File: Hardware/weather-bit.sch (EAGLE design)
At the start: 39 parts, among them J2 RJ11, J3 RJ11, U1 BME280, U2 micro:bit

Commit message: Updated One-Wire Hardware Set-up
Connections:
- removed net 13: U2.P13
- net 3.3V: now also R11.1; no longer R11.2
- net TEMP_DAT: now also R11.2, U2.P13; no longer R11.1
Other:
- moved on the sheet: J4, J5, J6, J7, R11

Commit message: Updating weather:bit per QC review
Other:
- note added: "v10"
- note removed: "v01"
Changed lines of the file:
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@@
 <sheet>
 <plain>
-<text x="238.76" y="7.62" size="2.54" layer="94">v01</text>
+<text x="238.76" y="7.62" size="2.54" layer="94">v10</text>
 <text x="5.08" y="175.26" size="5.08" layer="97">CONNECTOR</text>
 <text x="149.86" y="93.98" size="1.778" layer="97">20
@@
 <wire x1="58.42" y1="68.58" x2="58.42" y2="0" width="0.1524" layer="97" style="longdash"/>
 <text x="167.64" y="10.16" size="1.778" layer="94">Mary West, based on Weather Shield design by Nathan Seidle</text>
-<text x="241.3" y="7.62" size="1.778" layer="94">v01</text>
+<text x="241.3" y="7.62" size="1.778" layer="94">v10</text>
 </plain>
 <instances>

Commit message: Updated text in sch
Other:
- note added: "Intended to mate with OpenLog"
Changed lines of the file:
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@@
 <text x="167.64" y="10.16" size="1.778" layer="94">Mary West, based on Weather Shield design by Nathan Seidle</text>
 <text x="241.3" y="7.62" size="1.778" layer="94">v10</text>
+<text x="10.16" y="20.32" size="1.778" layer="97">Intended to mate with OpenLog</text>
 </plain>
 <instances>

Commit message: Added qwiic connector and logos
- added vertical qwiic connector near the 4-pin I2C header
- added qwiic logo near connector
- added big qwiic logos near product names on top and bottom silk
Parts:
- added J8: Qwiic (vertical), SparkFun-Connectors:QWIIC_CONNECTOR
- J9: value (none) -> PTH
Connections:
- net 3.3V: now also J8.2
- net GND: now also J8.1
- net SCL: now also J8.4
- net SDA: now also J8.3
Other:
- note added: "v11"
- moved on the sheet: J9

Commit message: SMD connector on 40 pin RA, and 4-pin I2C header
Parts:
- J6, J7: value (none) -> 455-1750-1-ND
- J9: value PTH -> 1X04_SMD_STRAIGHT_COMBO; device SparkFun-Connectors:CONN_041X04_NO_SILK -> SparkFun-Connectors:CONN_04SMD_STRAIGHT_COMBO
- U2: device Micro_Bit_Parts:MICRO:BITLEDS_UP -> SparkFun-Connectors:MICRO:BIT_RA
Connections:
- new net N$3: U2.P13
- net TEMP_DAT: no longer U2.P13

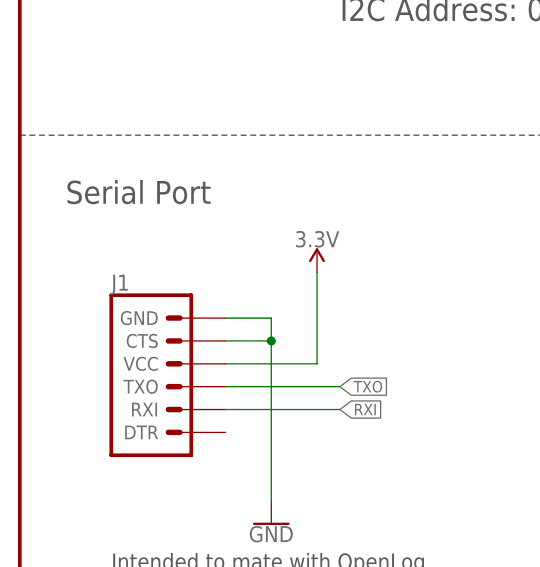
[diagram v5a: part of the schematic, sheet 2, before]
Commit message: Moved to SMT vertical female header for Serial port
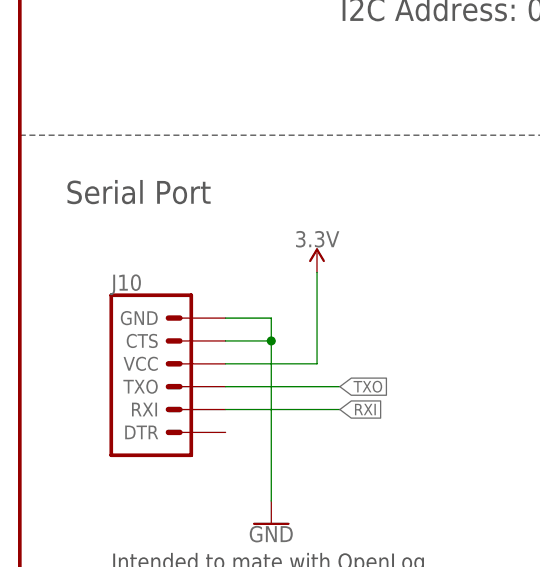
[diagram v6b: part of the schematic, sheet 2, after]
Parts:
- removed J1: (no value), SparkFun-Connectors:6_PIN_SERIAL_TARGETSILK
- added J10: (no value), SparkFun-Connectors:6_PIN_SERIAL_TARGETVERT_SMT
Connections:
- net 3.3V: now also J10.VCC; no longer J1.VCC
- net GND: now also J10.CTS, J10.GND; no longer J1.CTS, J1.GND
- net RXI: now also J10.RXI; no longer J1.RXI
- net TXO: now also J10.TXO; no longer J1.TXO
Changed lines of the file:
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@@
 <part name="SUPPLY8" library="SparkFun-PowerSymbols" deviceset="3.3V" device=""/>
 <part name="GND4" library="SparkFun-PowerSymbols" deviceset="GND" device=""/>
-<part name="J1" library="SparkFun-Connectors" deviceset="6_PIN_SERIAL_TARGET" device="SILK"/>
 <part name="SUPPLY1" library="SparkFun-PowerSymbols" deviceset="3.3V" device=""/>
 <part name="J8" library="SparkFun-Connectors" deviceset="QWIIC_CONNECTOR" device="" value="Qwiic (vertical)"/>
@@
 <part name="GND1" library="SparkFun-PowerSymbols" deviceset="GND" device=""/>
 <part name="U2" library="SparkFun-Connectors" deviceset="MICRO:BIT*?" device="_RA" value="micro:bit"/>
+<part name="J10" library="SparkFun-Connectors" deviceset="6_PIN_SERIAL_TARGET" device="VERT_SMT"/>
 </parts>
 <sheets>
@@
 <attribute name="VALUE" x="86.36" y="17.526" size="1.778" layer="96" align="top-center"/>
 </instance>
-<instance part="J1" gate="G$1" x="17.78" y="40.64" smashed="yes">
-<attribute name="VALUE" x="10.16" y="30.734" size="1.778" layer="96" font="vector"/>
-<attribute name="NAME" x="10.16" y="51.308" size="1.778" layer="95" font="vector"/>
-</instance>
 <instance part="SUPPLY1" gate="G$1" x="144.78" y="119.38" smashed="yes">
 <attribute name="VALUE" x="144.78" y="122.174" size="1.778" layer="96" align="bottom-center"/>
@@
 <instance part="GND1" gate="1" x="127" y="17.78" smashed="yes">
 <attribute name="VALUE" x="127" y="17.526" size="1.778" layer="96" align="top-center"/>
+</instance>
+<instance part="J10" gate="G$1" x="17.78" y="40.64" smashed="yes">
+<attribute name="VALUE" x="10.16" y="30.734" size="1.778" layer="96" font="vector"/>
+<attribute name="NAME" x="10.16" y="51.308" size="1.778" layer="95" font="vector"/>
 </instance>
 </instances>
@@
 </segment>
 <segment>
-<pinref part="J1" gate="G$1" pin="GND"/>
 <wire x1="22.86" y1="48.26" x2="27.94" y2="48.26" width="0.1524" layer="91"/>
 <wire x1="27.94" y1="48.26" x2="27.94" y2="45.72" width="0.1524" layer="91"/>
 <pinref part="GND2" gate="1" pin="GND"/>
-<pinref part="J1" gate="G$1" pin="CTS"/>
 <wire x1="27.94" y1="45.72" x2="27.94" y2="27.94" width="0.1524" layer="91"/>
 <wire x1="22.86" y1="45.72" x2="27.94" y2="45.72" width="0.1524" layer="91"/>
 <junction x="27.94" y="45.72"/>
+<pinref part="J10" gate="G$1" pin="CTS"/>
+<pinref part="J10" gate="G$1" pin="GND"/>
 </segment>
 <segment>
@@
 </segment>
 <segment>
-<pinref part="J1" gate="G$1" pin="VCC"/>
 <wire x1="22.86" y1="43.18" x2="33.02" y2="43.18" width="0.1524" layer="91"/>
 <pinref part="SUPPLY11" gate="G$1" pin="3.3V"/>
 <wire x1="33.02" y1="43.18" x2="33.02" y2="53.34" width="0.1524" layer="91"/>
+<pinref part="J10" gate="G$1" pin="VCC"/>
 </segment>
 <segment>
@@
 <net name="TXO" class="0">
 <segment>
-<pinref part="J1" gate="G$1" pin="TXO"/>
 <wire x1="22.86" y1="40.64" x2="35.56" y2="40.64" width="0.1524" layer="91"/>
 <label x="35.56" y="40.64" size="1.27" layer="95" font="vector" xref="yes"/>
+<pinref part="J10" gate="G$1" pin="TXO"/>
 </segment>
 </net>
 <net name="RXI" class="0">
 <segment>
-<pinref part="J1" gate="G$1" pin="RXI"/>
 <wire x1="22.86" y1="38.1" x2="35.56" y2="38.1" width="0.1524" layer="91"/>
 <label x="35.56" y="38.1" size="1.27" layer="95" font="vector" xref="yes"/>
-</segment>
-</net>
+<pinref part="J10" gate="G$1" pin="RXI"/>
+</segment>
+</net>

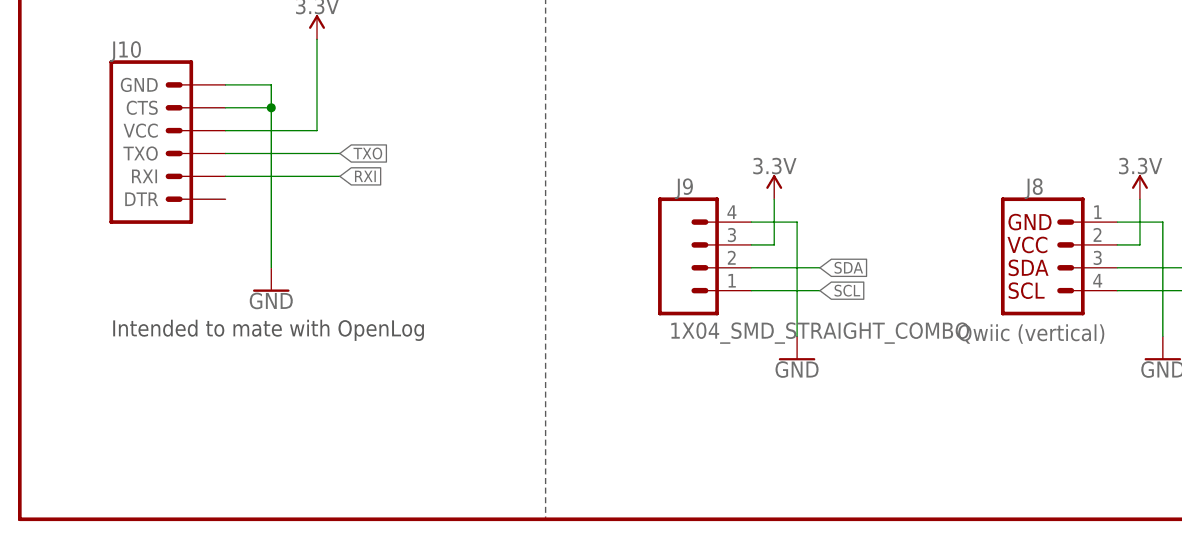
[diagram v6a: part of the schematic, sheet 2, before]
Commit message: SMT serial header and buzzard silk update
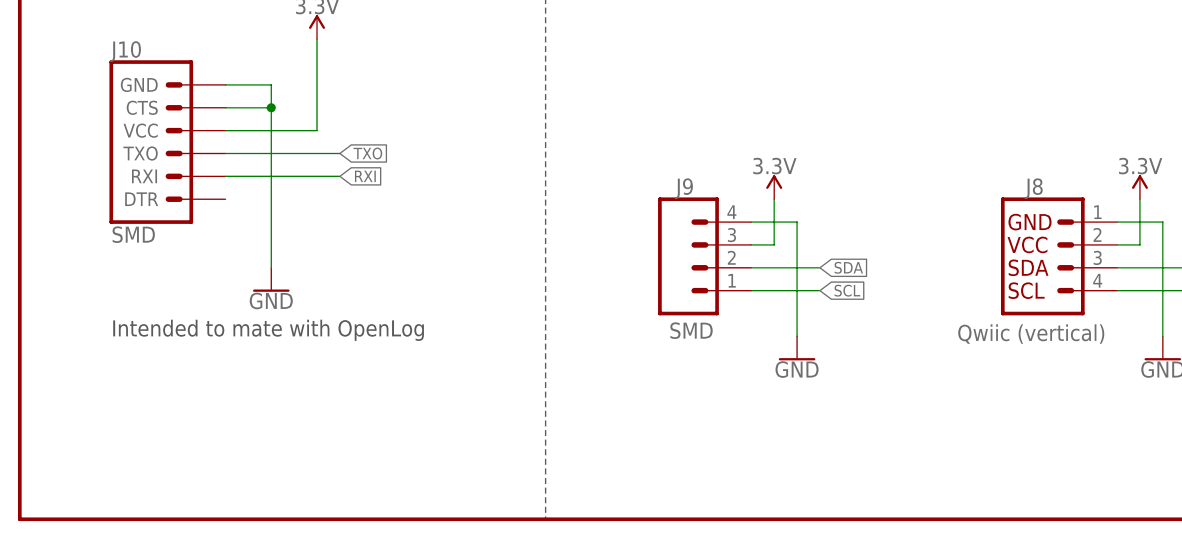
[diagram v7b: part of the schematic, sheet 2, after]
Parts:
- J10: value (none) -> SMD
- J9: value 1X04_SMD_STRAIGHT_COMBO -> SMD
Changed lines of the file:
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@@
 <part name="SUPPLY9" library="SparkFun-PowerSymbols" deviceset="3.3V" device=""/>
 <part name="SUPPLY10" library="SparkFun-PowerSymbols" deviceset="3.3V" device=""/>
-<part name="J9" library="SparkFun-Connectors" deviceset="CONN_04" device="SMD_STRAIGHT_COMBO" value="1X04_SMD_STRAIGHT_COMBO"/>
+<part name="J9" library="SparkFun-Connectors" deviceset="CONN_04" device="SMD_STRAIGHT_COMBO" value="SMD"/>
 <part name="SUPPLY11" library="SparkFun-PowerSymbols" deviceset="3.3V" device=""/>
 <part name="GND2" library="SparkFun-PowerSymbols" deviceset="GND" device=""/>
@@
 <part name="GND1" library="SparkFun-PowerSymbols" deviceset="GND" device=""/>
 <part name="U2" library="SparkFun-Connectors" deviceset="MICRO:BIT*?" device="_RA" value="micro:bit"/>
-<part name="J10" library="SparkFun-Connectors" deviceset="6_PIN_SERIAL_TARGET" device="VERT_SMT"/>
+<part name="J10" library="SparkFun-Connectors" deviceset="6_PIN_SERIAL_TARGET" device="VERT_SMT" value="SMD"/>
 </parts>
 <sheets>

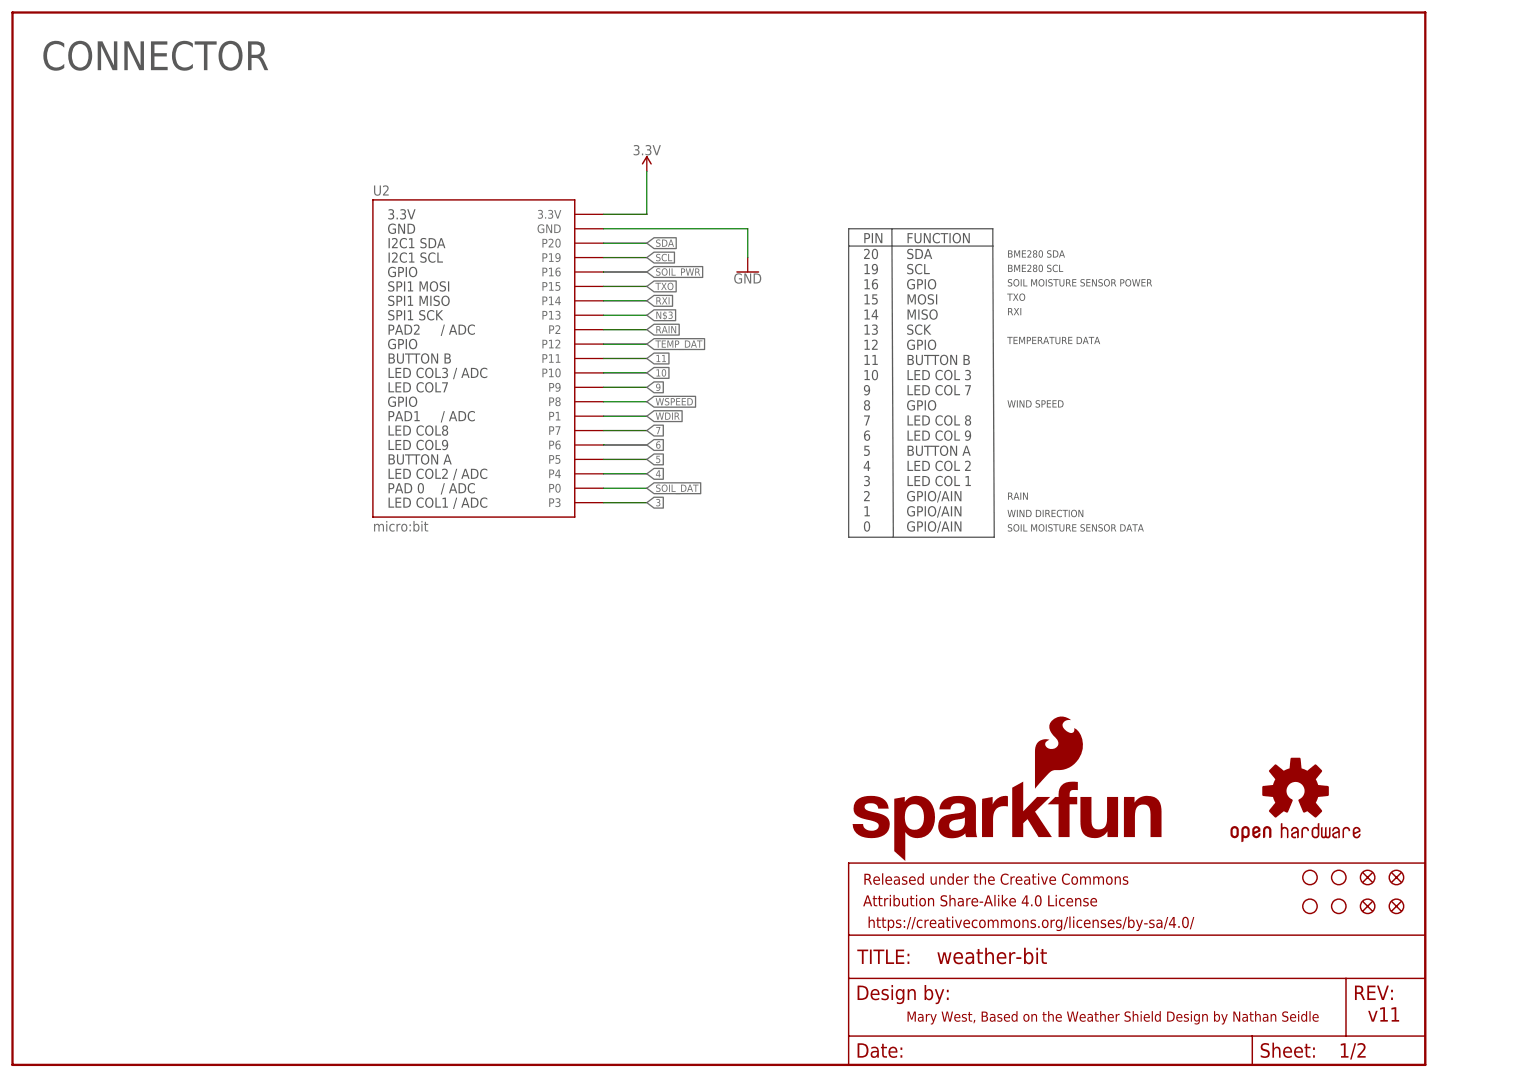
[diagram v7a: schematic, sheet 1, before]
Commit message: sch cleanup and move to one sheet
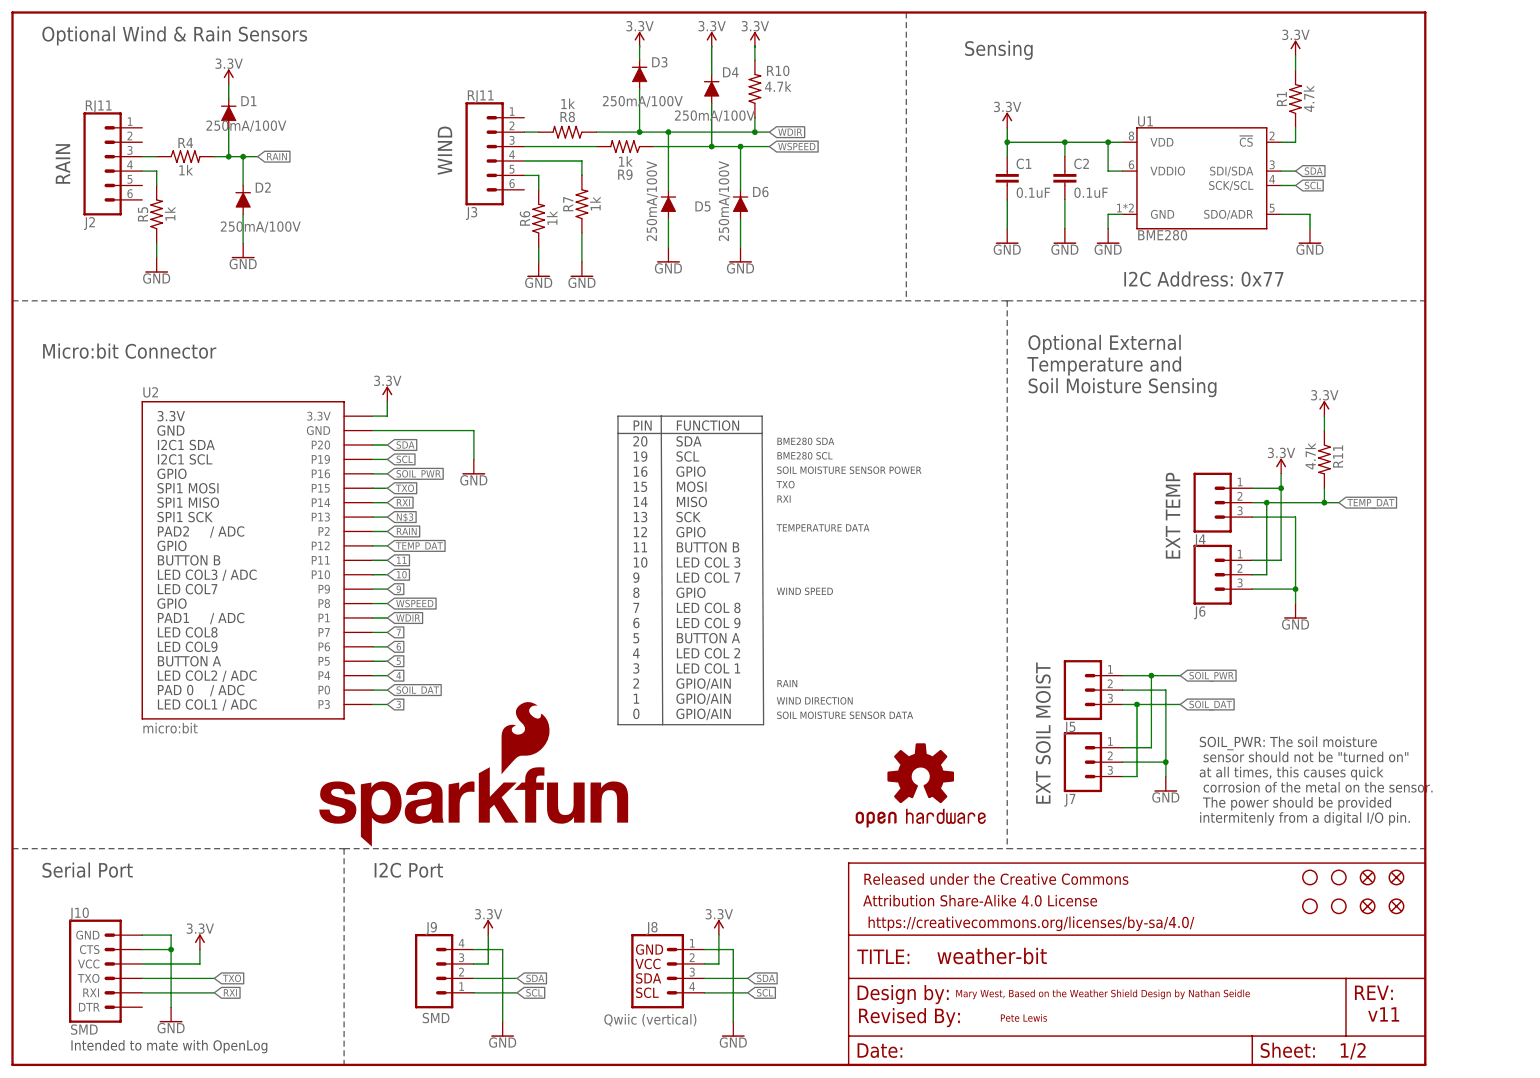
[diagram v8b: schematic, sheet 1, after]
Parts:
- removed FRAME2: FRAME-LETTER, SparkFun-Aesthetics:FRAME-LETTER
- J6, J7: value 455-1750-1-ND -> (none)
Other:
- note added: "Micro:bit Connector"
- note added: "Pete Lewis"
- note added: "Revised By:"
- note removed: "CONNECTOR"
- note removed: "Mary West, based on Weather Shield design by Nathan Seidle"
- note removed: "v10"
- moved on the sheet: U2
